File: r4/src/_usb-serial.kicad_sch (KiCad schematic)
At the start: 10 parts, among them U12 CP2102N-Axx-xQFN24

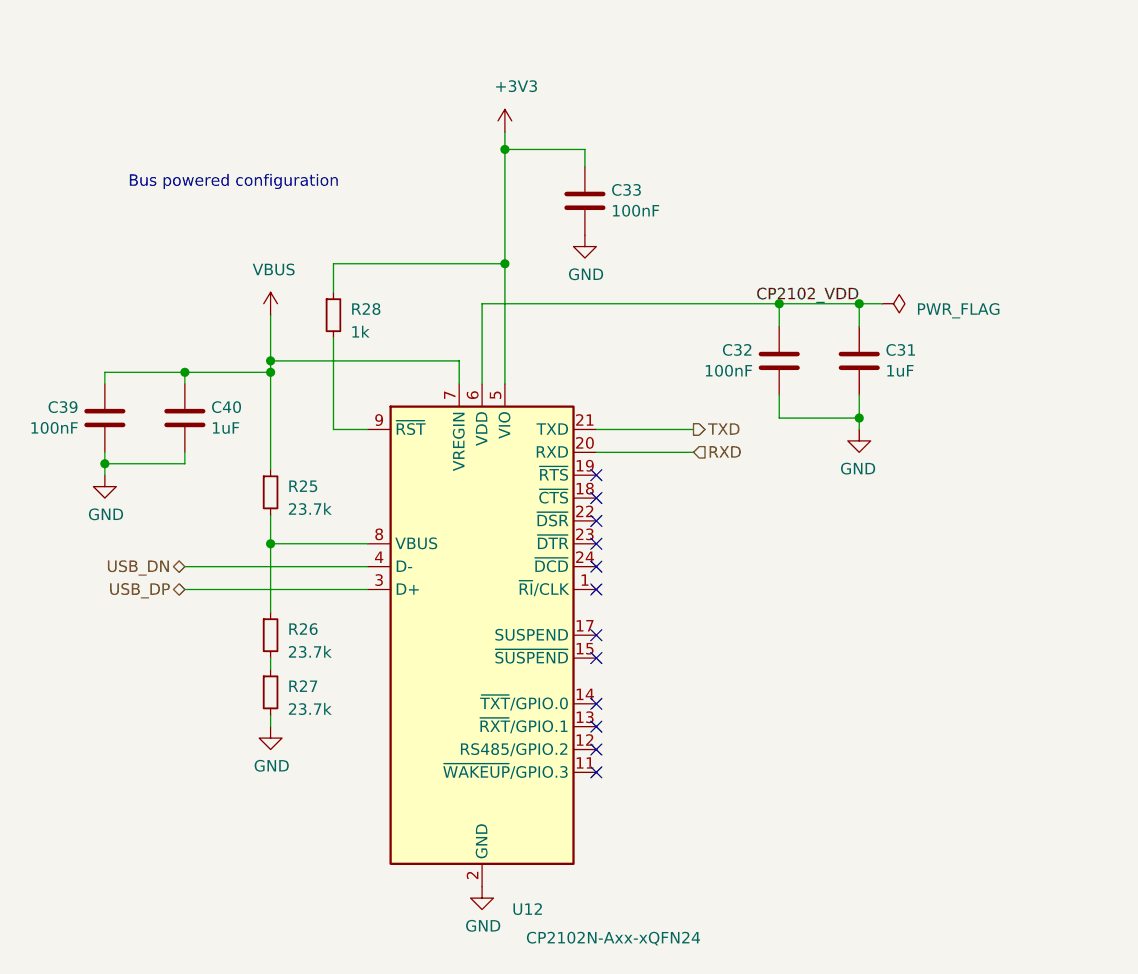
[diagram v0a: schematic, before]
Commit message: Update files to Kicad 6 format
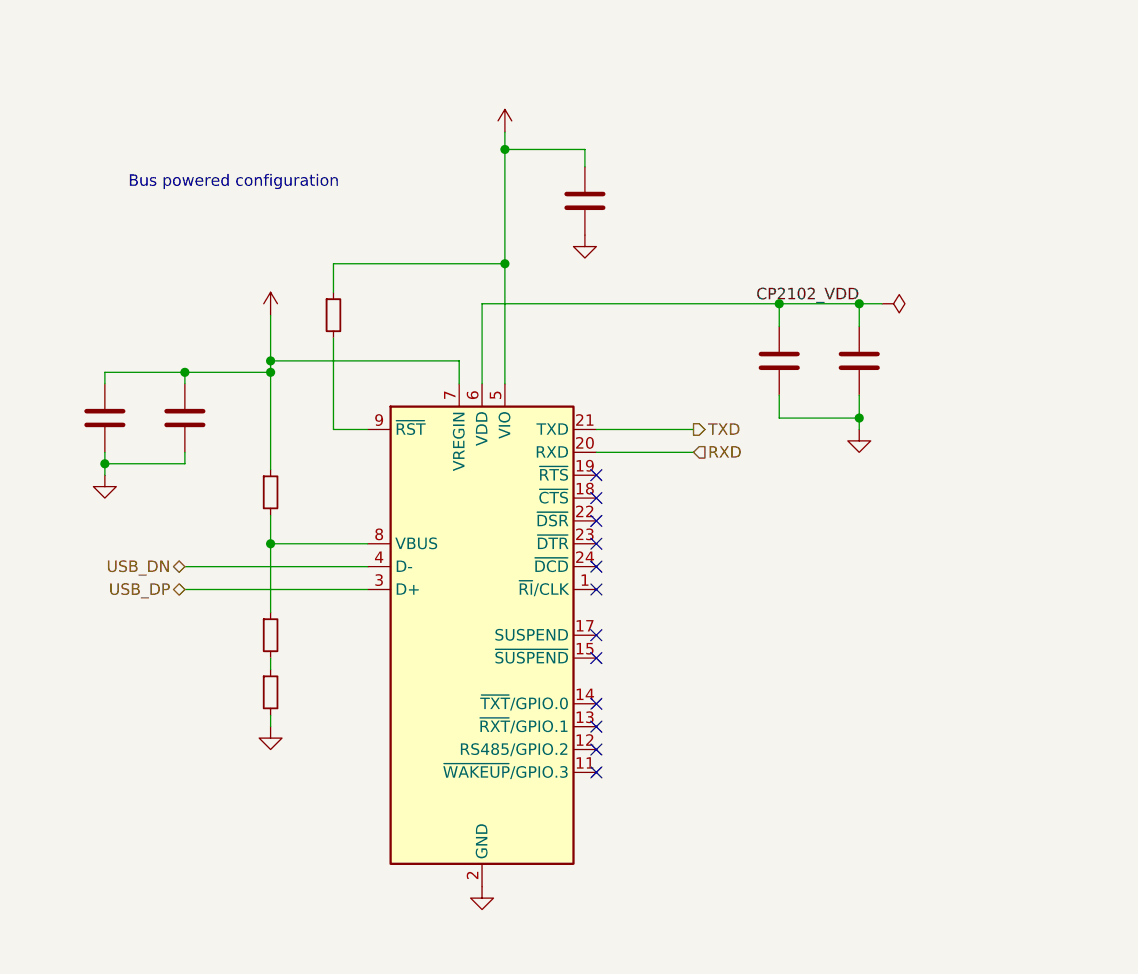
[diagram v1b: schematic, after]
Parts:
- ?: renamed from R28; value 1k -> (none); footprint Resistor_SMD:R_0603_1608Metric -> (none)
- ?: renamed from C33; value 100nF -> (none); footprint Capacitor_SMD:C_0603_1608Metric -> (none)
- ?: renamed from C39; value 100nF -> (none); footprint Capacitor_SMD:C_0603_1608Metric -> (none)
- ?: renamed from C32; value 100nF -> (none); footprint Capacitor_SMD:C_0603_1608Metric -> (none)
- ?: renamed from R26; value 23.7k -> (none); footprint Resistor_SMD:R_0603_1608Metric -> (none)
- ?: renamed from R25; value 23.7k -> (none); footprint Resistor_SMD:R_0603_1608Metric -> (none)
- ?: renamed from C40; value 1uF -> (none); footprint Capacitor_SMD:C_0603_1608Metric -> (none)
- ?: renamed from R27; value 23.7k -> (none); footprint Resistor_SMD:R_0603_1608Metric -> (none)
- ?: renamed from U12; value CP2102N-Axx-xQFN24 -> (none); footprint Package_DFN_QFN:QFN-24-1EP_4x4mm_P0.5mm_EP2.6x2.6mm -> (none)
- ?: renamed from C31; value 1uF -> (none); footprint Capacitor_SMD:C_0603_1608Metric -> (none)

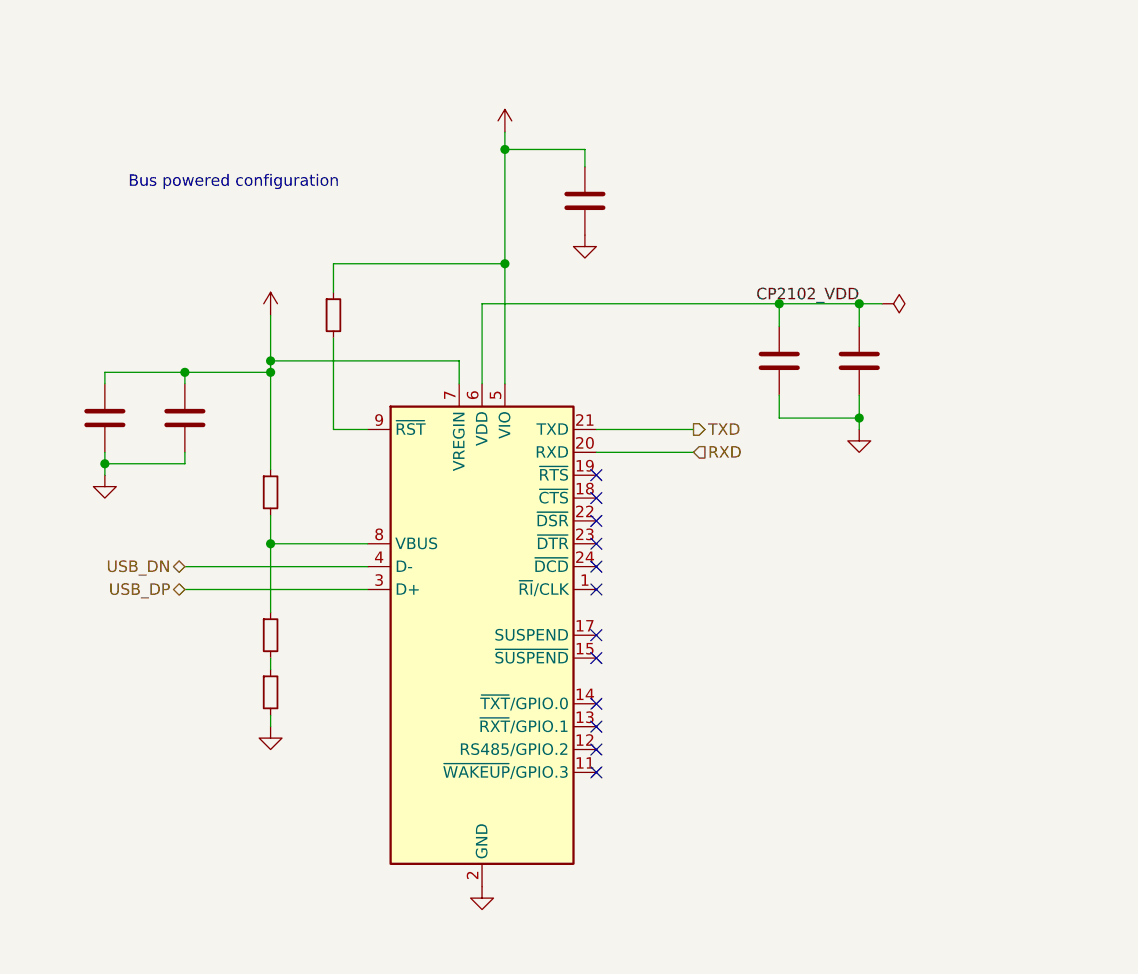
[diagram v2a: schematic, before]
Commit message: All grid misalignments fixed. Add electrolytics for bulk capacitance on +/- 15V rails
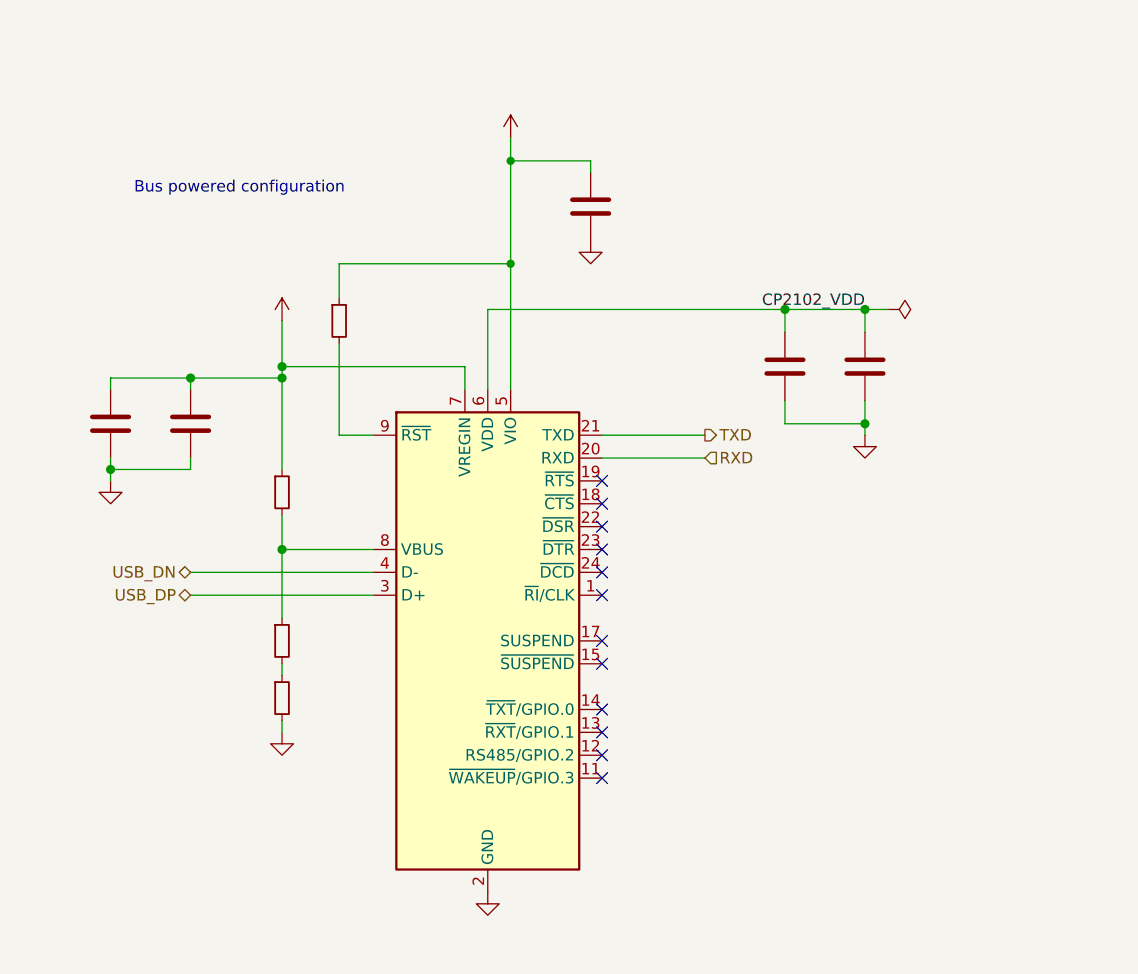
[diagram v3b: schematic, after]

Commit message: Add netclass definitions and assign nets. Define DRC rules to each class. Resize all vias and nets (with a few exceptions for very wide power tracks) to follow the netclass rules. Increase area for GNDA domain. Re-route SIM data bus around edge of GNDA domain
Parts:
- C31, C40: renamed from ?; value (none) -> 1uF; footprint (none) -> Capacitor_SMD:C_0603_1608Metric
- C32, C33, C39: renamed from ?; value (none) -> 100nF; footprint (none) -> Capacitor_SMD:C_0603_1608Metric
- R25, R26, R27: renamed from ?; value (none) -> 23.7k; footprint (none) -> Resistor_SMD:R_0603_1608Metric
- R28: renamed from ?; value (none) -> 1k; footprint (none) -> Resistor_SMD:R_0603_1608Metric
- U12: renamed from ?; value (none) -> CP2102N-Axx-xQFN24; footprint (none) -> Package_DFN_QFN:QFN-24-1EP_4x4mm_P0.5mm_EP2.6x2.6mm

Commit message: Set volage ratings on some caps, change some cap footprints to remove a couple of BOM lines
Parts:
- C31, C40: footprint Capacitor_SMD:C_0603_1608Metric -> Capacitor_SMD:C_0402_1005Metric
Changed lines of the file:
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@@
       (effects (font (size 1.27 1.27)) (justify left))
     )
-    (property "Footprint" "Capacitor_SMD:C_0603_1608Metric" (at 111.4552 90.17 0)
+    (property "Footprint" "Capacitor_SMD:C_0402_1005Metric" (at 111.4552 90.17 0)
       (effects (font (size 1.27 1.27)) hide)
     )
@@
       (project "bugg-main-r4"
         (path "/e3eb514f-6ce4-4abe-ba20-f82f0015628f/26331aa8-35b7-4c22-8a42-89230ada1085"
-          (reference "C40") (unit 1) (value "1uF") (footprint "Capacitor_SMD:C_0603_1608Metric")
+          (reference "C40") (unit 1) (value "1uF") (footprint "Capacitor_SMD:C_0402_1005Metric")
         )
       )
@@
       (effects (font (size 1.27 1.27)) (justify left))
     )
-    (property "Footprint" "Capacitor_SMD:C_0603_1608Metric" (at 186.3852 83.82 0)
+    (property "Footprint" "Capacitor_SMD:C_0402_1005Metric" (at 186.3852 83.82 0)
       (effects (font (size 1.27 1.27)) hide)
     )
@@
       (project "bugg-main-r4"
         (path "/e3eb514f-6ce4-4abe-ba20-f82f0015628f/26331aa8-35b7-4c22-8a42-89230ada1085"
-          (reference "C31") (unit 1) (value "1uF") (footprint "Capacitor_SMD:C_0603_1608Metric")
+          (reference "C31") (unit 1) (value "1uF") (footprint "Capacitor_SMD:C_0402_1005Metric")
         )
       )

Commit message: Route USB bus with 90ohm differential impedance assuming stackup configured in Kicad
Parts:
- C31, C40: Voltage (none) -> 6.3V
- C32, C33, C39: footprint Capacitor_SMD:C_0603_1608Metric -> Capacitor_SMD:C_0402_1005Metric
- R25, R26, R27, R28: footprint Resistor_SMD:R_0603_1608Metric -> Resistor_SMD:R_0402_1005Metric
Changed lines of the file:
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@@
       (effects (font (size 1.27 1.27)) (justify left))
     )
-    (property "Footprint" "Resistor_SMD:R_0603_1608Metric" (at 127 74.93 0)
+    (property "Footprint" "Resistor_SMD:R_0402_1005Metric" (at 127 74.93 0)
       (effects (font (size 1.27 1.27)) hide)
     )
@@
       (project "bugg-main-r4"
         (path "/e3eb514f-6ce4-4abe-ba20-f82f0015628f/26331aa8-35b7-4c22-8a42-89230ada1085"
-          (reference "R28") (unit 1) (value "1k") (footprint "Resistor_SMD:R_0603_1608Metric")
+          (reference "R28") (unit 1) (value "1k") (footprint "Resistor_SMD:R_0402_1005Metric")
         )
       )
@@
       (effects (font (size 1.27 1.27)) (justify left))
     )
-    (property "Footprint" "Capacitor_SMD:C_0603_1608Metric" (at 155.9052 66.04 0)
+    (property "Footprint" "Capacitor_SMD:C_0402_1005Metric" (at 155.9052 66.04 0)
       (effects (font (size 1.27 1.27)) hide)
     )
@@
       (project "bugg-main-r4"
         (path "/e3eb514f-6ce4-4abe-ba20-f82f0015628f/26331aa8-35b7-4c22-8a42-89230ada1085"
-          (reference "C33") (unit 1) (value "100nF") (footprint "Capacitor_SMD:C_0603_1608Metric")
+          (reference "C33") (unit 1) (value "100nF") (footprint "Capacitor_SMD:C_0402_1005Metric")
         )
       )
@@
       (effects (font (size 1.27 1.27)) (justify left))
     )
-    (property "Footprint" "Capacitor_SMD:C_0603_1608Metric" (at 100.6348 90.17 0)
+    (property "Footprint" "Capacitor_SMD:C_0402_1005Metric" (at 100.6348 90.17 0)
       (effects (font (size 1.27 1.27)) hide)
     )
@@
       (project "bugg-main-r4"
         (path "/e3eb514f-6ce4-4abe-ba20-f82f0015628f/26331aa8-35b7-4c22-8a42-89230ada1085"
-          (reference "C39") (unit 1) (value "100nF") (footprint "Capacitor_SMD:C_0603_1608Metric")
+          (reference "C39") (unit 1) (value "100nF") (footprint "Capacitor_SMD:C_0402_1005Metric")
         )
       )
@@
       (effects (font (size 1.27 1.27)) (justify left))
     )
-    (property "Footprint" "Capacitor_SMD:C_0603_1608Metric" (at 175.5648 83.82 0)
+    (property "Footprint" "Capacitor_SMD:C_0402_1005Metric" (at 175.5648 83.82 0)
       (effects (font (size 1.27 1.27)) hide)
     )
@@
       (project "bugg-main-r4"
         (path "/e3eb514f-6ce4-4abe-ba20-f82f0015628f/26331aa8-35b7-4c22-8a42-89230ada1085"
-          (reference "C32") (unit 1) (value "100nF") (footprint "Capacitor_SMD:C_0603_1608Metric")
+          (reference "C32") (unit 1) (value "100nF") (footprint "Capacitor_SMD:C_0402_1005Metric")
         )
       )
@@
       (effects (font (size 1.27 1.27)) (justify left))
     )
-    (property "Footprint" "Resistor_SMD:R_0603_1608Metric" (at 120.65 110.49 0)
+    (property "Footprint" "Resistor_SMD:R_0402_1005Metric" (at 120.65 110.49 0)
       (effects (font (size 1.27 1.27)) hide)
     )
@@
       (project "bugg-main-r4"
         (path "/e3eb514f-6ce4-4abe-ba20-f82f0015628f/26331aa8-35b7-4c22-8a42-89230ada1085"
-          (reference "R26") (unit 1) (value "23.7k") (footprint "Resistor_SMD:R_0603_1608Metric")
+          (reference "R26") (unit 1) (value "23.7k") (footprint "Resistor_SMD:R_0402_1005Metric")
         )
       )
@@
       (effects (font (size 1.27 1.27)) (justify left))
     )
-    (property "Footprint" "Resistor_SMD:R_0603_1608Metric" (at 120.65 93.98 0)
+    (property "Footprint" "Resistor_SMD:R_0402_1005Metric" (at 120.65 93.98 0)
       (effects (font (size 1.27 1.27)) hide)
     )
@@
       (project "bugg-main-r4"
         (path "/e3eb514f-6ce4-4abe-ba20-f82f0015628f/26331aa8-35b7-4c22-8a42-89230ada1085"
-          (reference "R25") (unit 1) (value "23.7k") (footprint "Resistor_SMD:R_0603_1608Metric")
+          (reference "R25") (unit 1) (value "23.7k") (footprint "Resistor_SMD:R_0402_1005Metric")
         )
       )
@@
       (effects (font (size 1.27 1.27)) hide)
     )
+    (property "Voltage" "6.3V" (at 110.49 86.36 0)
+      (effects (font (size 1.27 1.27)) hide)
+    )
     (pin "1")
     (pin "2")
@@
       (effects (font (size 1.27 1.27)) (justify left))
     )
-    (property "Footprint" "Resistor_SMD:R_0603_1608Metric" (at 120.65 116.84 0)
+    (property "Footprint" "Resistor_SMD:R_0402_1005Metric" (at 120.65 116.84 0)
       (effects (font (size 1.27 1.27)) hide)
     )
@@
       (project "bugg-main-r4"
         (path "/e3eb514f-6ce4-4abe-ba20-f82f0015628f/26331aa8-35b7-4c22-8a42-89230ada1085"
-          (reference "R27") (unit 1) (value "23.7k") (footprint "Resistor_SMD:R_0603_1608Metric")
+          (reference "R27") (unit 1) (value "23.7k") (footprint "Resistor_SMD:R_0402_1005Metric")
         )
       )
@@
       (effects (font (size 1.27 1.27)) hide)
     )
+    (property "Voltage" "6.3V" (at 185.42 80.01 0)
+      (effects (font (size 1.27 1.27)) hide)
+    )

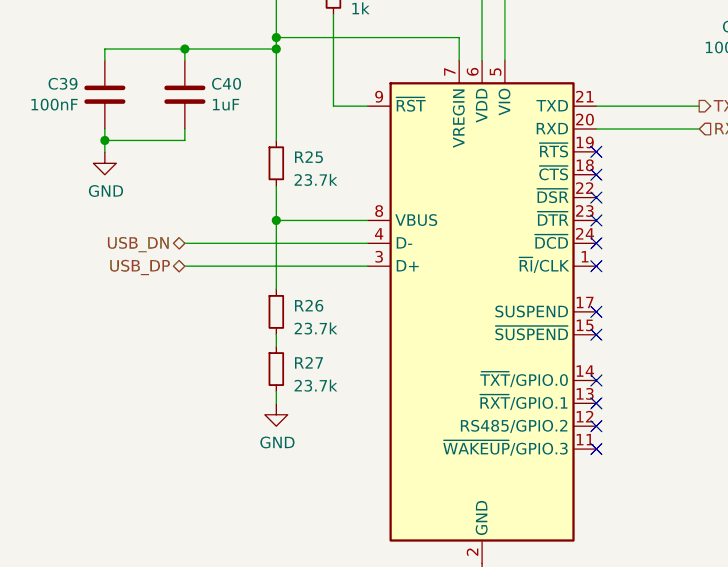
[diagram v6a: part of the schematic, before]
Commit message: Change some passive values and packages to get rid of some BOM lines
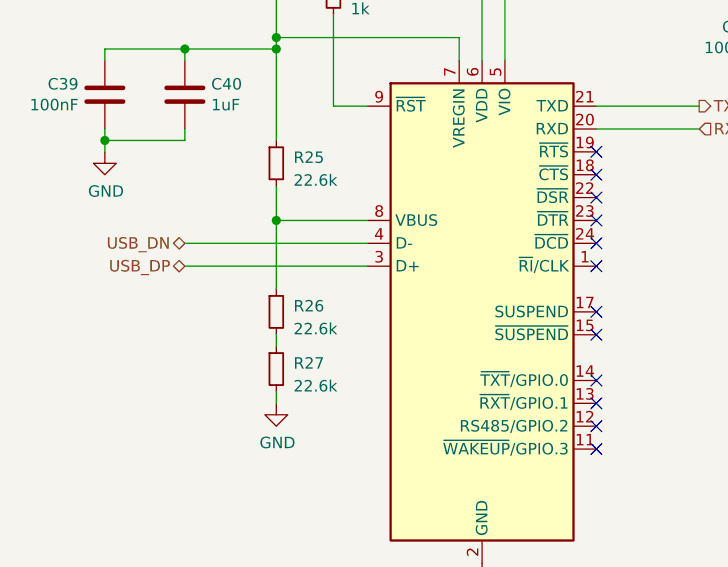
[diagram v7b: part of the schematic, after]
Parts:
- R25, R26, R27: value 23.7k -> 22.6k
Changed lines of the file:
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@@
       (effects (font (size 1.27 1.27)) (justify left))
     )
-    (property "Value" "23.7k" (at 122.555 112.395 0)
+    (property "Value" "22.6k" (at 122.555 112.395 0)
       (effects (font (size 1.27 1.27)) (justify left))
     )
@@
       (project "bugg-main-r4"
         (path "/e3eb514f-6ce4-4abe-ba20-f82f0015628f/26331aa8-35b7-4c22-8a42-89230ada1085"
-          (reference "R26") (unit 1) (value "23.7k") (footprint "Resistor_SMD:R_0402_1005Metric")
+          (reference "R26") (unit 1) (value "22.6k") (footprint "Resistor_SMD:R_0402_1005Metric")
         )
       )
@@
       (effects (font (size 1.27 1.27)) (justify left))
     )
-    (property "Value" "23.7k" (at 122.555 95.885 0)
+    (property "Value" "22.6k" (at 122.555 95.885 0)
       (effects (font (size 1.27 1.27)) (justify left))
     )
@@
       (project "bugg-main-r4"
         (path "/e3eb514f-6ce4-4abe-ba20-f82f0015628f/26331aa8-35b7-4c22-8a42-89230ada1085"
-          (reference "R25") (unit 1) (value "23.7k") (footprint "Resistor_SMD:R_0402_1005Metric")
+          (reference "R25") (unit 1) (value "22.6k") (footprint "Resistor_SMD:R_0402_1005Metric")
         )
       )
@@
       (effects (font (size 1.27 1.27)) (justify left))
     )
-    (property "Value" "23.7k" (at 122.555 118.745 0)
+    (property "Value" "22.6k" (at 122.555 118.745 0)
       (effects (font (size 1.27 1.27)) (justify left))
     )
@@
       (project "bugg-main-r4"
         (path "/e3eb514f-6ce4-4abe-ba20-f82f0015628f/26331aa8-35b7-4c22-8a42-89230ada1085"
-          (reference "R27") (unit 1) (value "23.7k") (footprint "Resistor_SMD:R_0402_1005Metric")
+          (reference "R27") (unit 1) (value "22.6k") (footprint "Resistor_SMD:R_0402_1005Metric")
         )
       )
